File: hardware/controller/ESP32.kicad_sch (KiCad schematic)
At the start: 1 part, among them U1 ESP32-S3

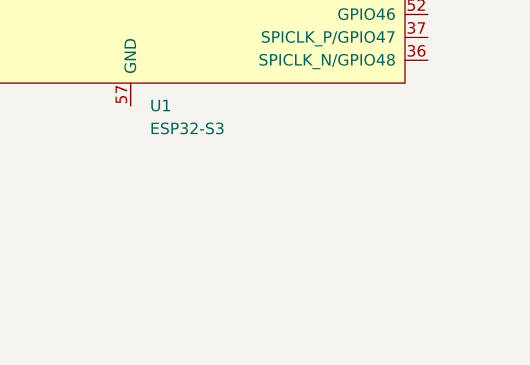
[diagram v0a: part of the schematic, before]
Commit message: added LED IC's and USB UART bridge
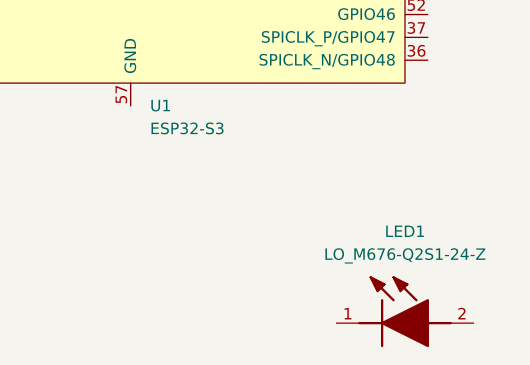
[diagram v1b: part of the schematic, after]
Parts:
- added LED1: LO_M676-Q2S1-24-Z, LEDM2214X140N, symbol SamacSys_Parts:LO_M676-Q2S1-24-Z
- U1: Manufacturer_Part_Number (none) -> ESP32-S3; Mouser Part Number (none) -> 356-ESP32-S3; Mouser Price/Stock (none) -> https://www.mouser.co.uk/ProductDetail/Espressif-Systems/ES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
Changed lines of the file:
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@@
 	(paper "A4")
+	(symbol
+		(lib_id "SamacSys_Parts:LO_M676-Q2S1-24-Z")
+		(at 146.05 153.67 0)
+		(unit 1)
+		(exclude_from_sim no)
+		(in_bom yes)
+		(on_board yes)
+		(dnp no)
+		(fields_autoplaced yes)
+		(property "Reference" "LED1"
+			(at 153.67 143.51 0)
+			(effects
+				(font
+					(size 1.27 1.27)
+				)
+			)
+		)
+		(property "Value" "LO_M676-Q2S1-24-Z"
+			(at 153.67 146.05 0)
+			(effects
+				(font
+					(size 1.27 1.27)
+				)
+			)
+		)
+		(property "Footprint" "LEDM2214X140N"
+			(at 158.75 247.32 0)
+			(effects
+				(font
+					(size 1.27 1.27)
+				)
+				(justify left bottom)
+				(hide yes)
+			)
+		)
+		(property "Datasheet" "https://www.mouser.in/datasheet/2/588/Osram_7222021_LY__M676_EN-2891431.pdf"
+			(at 158.75 347.32 0)
+			(effects
+				(font
+					(size 1.27 1.27)
+				)
+				(justify left bottom)
+				(hide yes)
+			)
+		)
+		(property "Description" "Standard LEDs - SMD Orange, 606nm 224mcd, 20mA"
+			(at 146.05 153.67 0)
+			(effects
+				(font
+					(size 1.27 1.27)
+				)
+				(hide yes)
+			)
+		)
+		(property "Height" "1.4"
+			(at 158.75 547.32 0)
+			(effects
+				(font
+					(size 1.27 1.27)
+				)
+				(justify left bottom)
+				(hide yes)
+			)
+		)
+		(property "Mouser Part Number" "720-LOM676Q2S124Z"
+			(at 158.75 647.32 0)
+			(effects
+				(font
+					(size 1.27 1.27)
+				)
+				(justify left bottom)
+				(hide yes)
+			)
+		)
+		(property "Mouser Price/Stock" "https://www.mouser.co.uk/ProductDetail/OSRAM-Opto-Semiconductors/LO-M676-Q2S1-24-Z?qs=nTDll3UaDK6JlNmxoQCpEQ%3D%3D"
+			(at 158.75 747.32 0)
+			(effects
+				(font
+					(size 1.27 1.27)
+				)
+				(justify left bottom)
+				(hide yes)
+			)
+		)
+		(property "Manufacturer_Name" "ams OSRAM"
+			(at 158.75 847.32 0)
+			(effects
+				(font
+					(size 1.27 1.27)
+				)
+				(justify left bottom)
+				(hide yes)
+			)
+		)
+		(property "Manufacturer_Part_Number" "LO M676-Q2S1-24-Z"
+			(at 158.75 947.32 0)
+			(effects
+				(font
+					(size 1.27 1.27)
+				)
+				(justify left bottom)
+				(hide yes)
+			)
+		)
+		(pin "2"
+		)
+		(pin "1"
+		)
+		(instances
+			(project ""
+				(path "/869bea87-c885-4ead-826b-3f34ceacafad/803675b3-25f7-4b49-b465-4697774a1dce"
+					(reference "LED1")
+					(unit 1)
+				)
+			)
+		)
+	)
 	(symbol
 		(lib_id "Espressif:ESP32-S3")
@@
 			)
 		)
+		(property "Mouser Part Number" "356-ESP32-S3"
+			(at 123.19 88.9 0)
+			(effects
+				(font
+					(size 1.27 1.27)
+				)
+				(hide yes)
+			)
+		)
+		(property "Mouser Price/Stock" "https://www.mouser.co.uk/ProductDetail/Espressif-Systems/ESP32-S3?qs=Rp5uXu7WBW%2FNWuUy%252BBihNw%3D%3D"
+			(at 123.19 88.9 0)
+			(effects
+				(font
+					(size 1.27 1.27)
+				)
+				(hide yes)
+			)
+		)
+		(property "Manufacturer_Part_Number" "ESP32-S3"
+			(at 123.19 88.9 0)
+			(effects
+				(font
+					(size 1.27 1.27)
+				)
+				(hide yes)
+			)
+		)
 		(pin "37"
 		)
@@
 					(unit 1)
 				)
-				(path "/869bea87-c885-4ead-826b-3f34ceacafad/cc3ab021-ec15-450e-9af3-a840a920a1aa"
-					(reference "U4")
-					(unit 1)
-				)

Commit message: asdasd
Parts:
- removed LED1: LO_M676-Q2S1-24-Z, LEDM2214X140N, symbol SamacSys_Parts:LO_M676-Q2S1-24-Z
- renumbered U1 to U2
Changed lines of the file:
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@@
 	(paper "A4")
-	(symbol
-		(lib_id "SamacSys_Parts:LO_M676-Q2S1-24-Z")
-		(at 146.05 153.67 0)
-		(unit 1)
-		(exclude_from_sim no)
-		(in_bom yes)
-		(on_board yes)
-		(dnp no)
-		(fields_autoplaced yes)
-		(property "Reference" "LED1"
-			(at 153.67 143.51 0)
-			(effects
-				(font
-					(size 1.27 1.27)
-				)
-			)
-		)
-		(property "Value" "LO_M676-Q2S1-24-Z"
-			(at 153.67 146.05 0)
-			(effects
-				(font
-					(size 1.27 1.27)
-				)
-			)
-		)
-		(property "Footprint" "LEDM2214X140N"
-			(at 158.75 247.32 0)
-			(effects
-				(font
-					(size 1.27 1.27)
-				)
-				(justify left bottom)
-				(hide yes)
-			)
-		)
-		(property "Datasheet" "https://www.mouser.in/datasheet/2/588/Osram_7222021_LY__M676_EN-2891431.pdf"
-			(at 158.75 347.32 0)
-			(effects
-				(font
-					(size 1.27 1.27)
-				)
-				(justify left bottom)
-				(hide yes)
-			)
-		)
-		(property "Description" "Standard LEDs - SMD Orange, 606nm 224mcd, 20mA"
-			(at 146.05 153.67 0)
-			(effects
-				(font
-					(size 1.27 1.27)
-				)
-				(hide yes)
-			)
-		)
-		(property "Height" "1.4"
-			(at 158.75 547.32 0)
-			(effects
-				(font
-					(size 1.27 1.27)
-				)
-				(justify left bottom)
-				(hide yes)
-			)
-		)
-		(property "Mouser Part Number" "720-LOM676Q2S124Z"
-			(at 158.75 647.32 0)
-			(effects
-				(font
-					(size 1.27 1.27)
-				)
-				(justify left bottom)
-				(hide yes)
-			)
-		)
-		(property "Mouser Price/Stock" "https://www.mouser.co.uk/ProductDetail/OSRAM-Opto-Semiconductors/LO-M676-Q2S1-24-Z?qs=nTDll3UaDK6JlNmxoQCpEQ%3D%3D"
-			(at 158.75 747.32 0)
-			(effects
-				(font
-					(size 1.27 1.27)
-				)
-				(justify left bottom)
-				(hide yes)
-			)
-		)
-		(property "Manufacturer_Name" "ams OSRAM"
-			(at 158.75 847.32 0)
-			(effects
-				(font
-					(size 1.27 1.27)
-				)
-				(justify left bottom)
-				(hide yes)
-			)
-		)
-		(property "Manufacturer_Part_Number" "LO M676-Q2S1-24-Z"
-			(at 158.75 947.32 0)
-			(effects
-				(font
-					(size 1.27 1.27)
-				)
-				(justify left bottom)
-				(hide yes)
-			)
-		)
-		(pin "2"
-		)
-		(pin "1"
-		)
-		(instances
-			(project ""
-				(path "/869bea87-c885-4ead-826b-3f34ceacafad/803675b3-25f7-4b49-b465-4697774a1dce"
-					(reference "LED1")
-					(unit 1)
-				)
-			)
-		)
-	)
 	(symbol
 		(lib_id "Espressif:ESP32-S3")
@@
 		(dnp no)
 		(fields_autoplaced yes)
-		(property "Reference" "U1"
+		(property "Reference" "U2"
 			(at 125.3333 129.54 0)
 			(effects
@@
 			(project "controller"
 				(path "/869bea87-c885-4ead-826b-3f34ceacafad/803675b3-25f7-4b49-b465-4697774a1dce"
-					(reference "U1")
+					(reference "U2")
 					(unit 1)
 				)

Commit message: a
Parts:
- added AE1: Antenna_Chip, symbol Device:Antenna_Chip
- added C1, C4, C5, C6: 0u1, symbol Device:C
- added C11, C12: 1p8, symbol Device:C
- added C2: 10u, symbol Device:C
- added C3, C7: 1u, symbol Device:C
- added C8, C9: 10p, symbol Device:C
- added J5: Conn_01x04_Pin, symbol Connector:Conn_01x04_Pin
- added L1: 2nH, symbol Device:L
- added L2: 24n, symbol Device:L
- added L4: 3nH, symbol Device:L
- added Q1, Q2: SS8050-G, SOT95P240X115-3N, symbol SamacSys_Parts:SS8050-G
- added R23, R24: 10k, symbol Device:R
- added Y2: FH4000074Z, FH4000074Z, symbol SamacSys_Parts:FH4000074Z
- U2: symbol Espressif:ESP32-S3 -> SamacSys_Parts:ESP32-S3
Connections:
- net VDD3P3: now also C5.1, L1.2
- net at U2.1 (LNA_IN/RF): now also C12.1, L4.2
- net +3V3: now reaches U2.20 (VDD3P3_RTC)
- net +3V3: now also U2.55 (VDDA), U2.56 (VDDA), C1.1, C2.1, C3.1, C4.1, L1.1
- net VDD_SPI: now reaches U2.29 (VDD_SPI)
- net VDD_SPI: now also C6.1, C7.1
- net CHIP_PU: now reaches U2.4 (CHIP_PU/RESET)
- net MTCK: now reaches U2.44 (MTCK/JTAG/GPIO39)
- net MTCK: now also J5.4 (Pin_4)
- net MTDO: now reaches U2.45 (MTDO/JTAG/GPIO40)
- net MTDO: now also J5.3 (Pin_3)
- net at U2.46 (VDD3P3_CPU): now also C1.2
- net MTDI: now reaches U2.47 (MTDI/JTAG/GPIO41)
- net MTDI: now also J5.2 (Pin_2)
- net MTMS: now reaches U2.48 (MTMS/JTAG/GPIO42)
- net MTMS: now also J5.1 (Pin_1)
- net at U2.53 (XTAL_N): now also C8.1, Y2.3 (XOUT)
- net at U2.54 (XTAL_P): now also L2.2
- net GND: now reaches U2.57 (GND)
- net GND: now also AE1.1 (FEED), C11.2, C12.2, C2.2, C3.2, C4.2, C5.2, C6.2, C7.2, C8.2, C9.2, Y2.2 (GND), Y2.4 (GND)
- new net: Q2.1 (B), R24.2
- new net: AE1.2 (PCB_Trace), C11.1, L4.1
- new net: C9.1, L2.1, Y2.1 (XIN)
- new net: Q1.1 (B), R23.2
- new net DTR: Q1.3 (C), R24.1
- new net EN: Q2.3 (C)
- new net IO0: Q1.2 (E)
- new net RTS: Q2.2 (E), R23.1
- no-connect marks 0 -> 2
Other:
- note added: "Auto-flash"
- note added: "JTAG Interface"
- note added: "todo: expose jtag port"
- note added: "todo: look into why some of these power pins do not hvae any decouplihg caps"
- moved on the sheet: U2

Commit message: fixed bus stuff
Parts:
- renumbered C8 to C1, C5 to C10, C1 to C11, C9 to C2, C2 to C3, C11 to C4, C12 to C5, C3 to C6, C6 to C7, C4 to C8, C7 to C9, J5 to J4, L4 to L1, L1 to L3, Q2 to Q1, Q1 to Q2, R23 to R10, R24 to R9, Y2 to Y1
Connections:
- net BUT_JOY.BUT_DOWN: now also U2.15 (GPIO10/ADC1_CH9)
- net BUT_JOY.BUT_LEFT: now also U2.12 (GPIO7/ADC1_CH6)
- net BUT_JOY.BUT_RIGHT: now also U2.13 (GPIO8/ADC1_CH7)
- net BUT_JOY.BUT_UP: now also U2.14 (GPIO9/ADC1_CH8)
- net BUT_JOY.JOY1_H: now also U2.11 (GPIO6/ADC1_CH5)
- net BUT_JOY.JOY1_V: now also U2.10 (GPIO5/ADC1_CH4)
- net BUT_JOY.JOY2_H: now also U2.9 (GPIO4/ADC1_CH3)
- net BUT_JOY.JOY2_V: now also U2.8 (GPIO3/ADC1_CH2)
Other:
- note added: "JTAG Interface Male Headers"
- note removed: "JTAG Interface"
- moved on the sheet: J4

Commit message: bussin
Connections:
- net RXD: now also U2.50 (U0RXD/PROG/GPIO44)
- net TXD: now also U2.49 (U0TXD/PROG/GPIO43)
- net ~{CE}: now reaches U2.28 (SPI_CS1/GPIO26)
- net DQ3: now reaches U2.30 (SPIHD/GPIO27)
- net DQ2: now reaches U2.31 (SPIWP/GPIO28)
- net ~{CS}: now reaches U2.32 (SPICS0/GPIO29)
- net OPI_CLK: now reaches U2.33 (SPICLK/GPIO30)
- net DQ1: now reaches U2.34 (SPIQ/GPIO31)
- net DQ0: now reaches U2.35 (SPID/GPIO32)
- net DQ4: now reaches U2.38 (GPIO33)
- net DQ5: now reaches U2.39 (GPIO34)
- net DQ6: now reaches U2.40 (GPIO35)
- net DQ7: now reaches U2.41 (GPIO36)
- net DQS/DM: now reaches U2.42 (GPIO37)

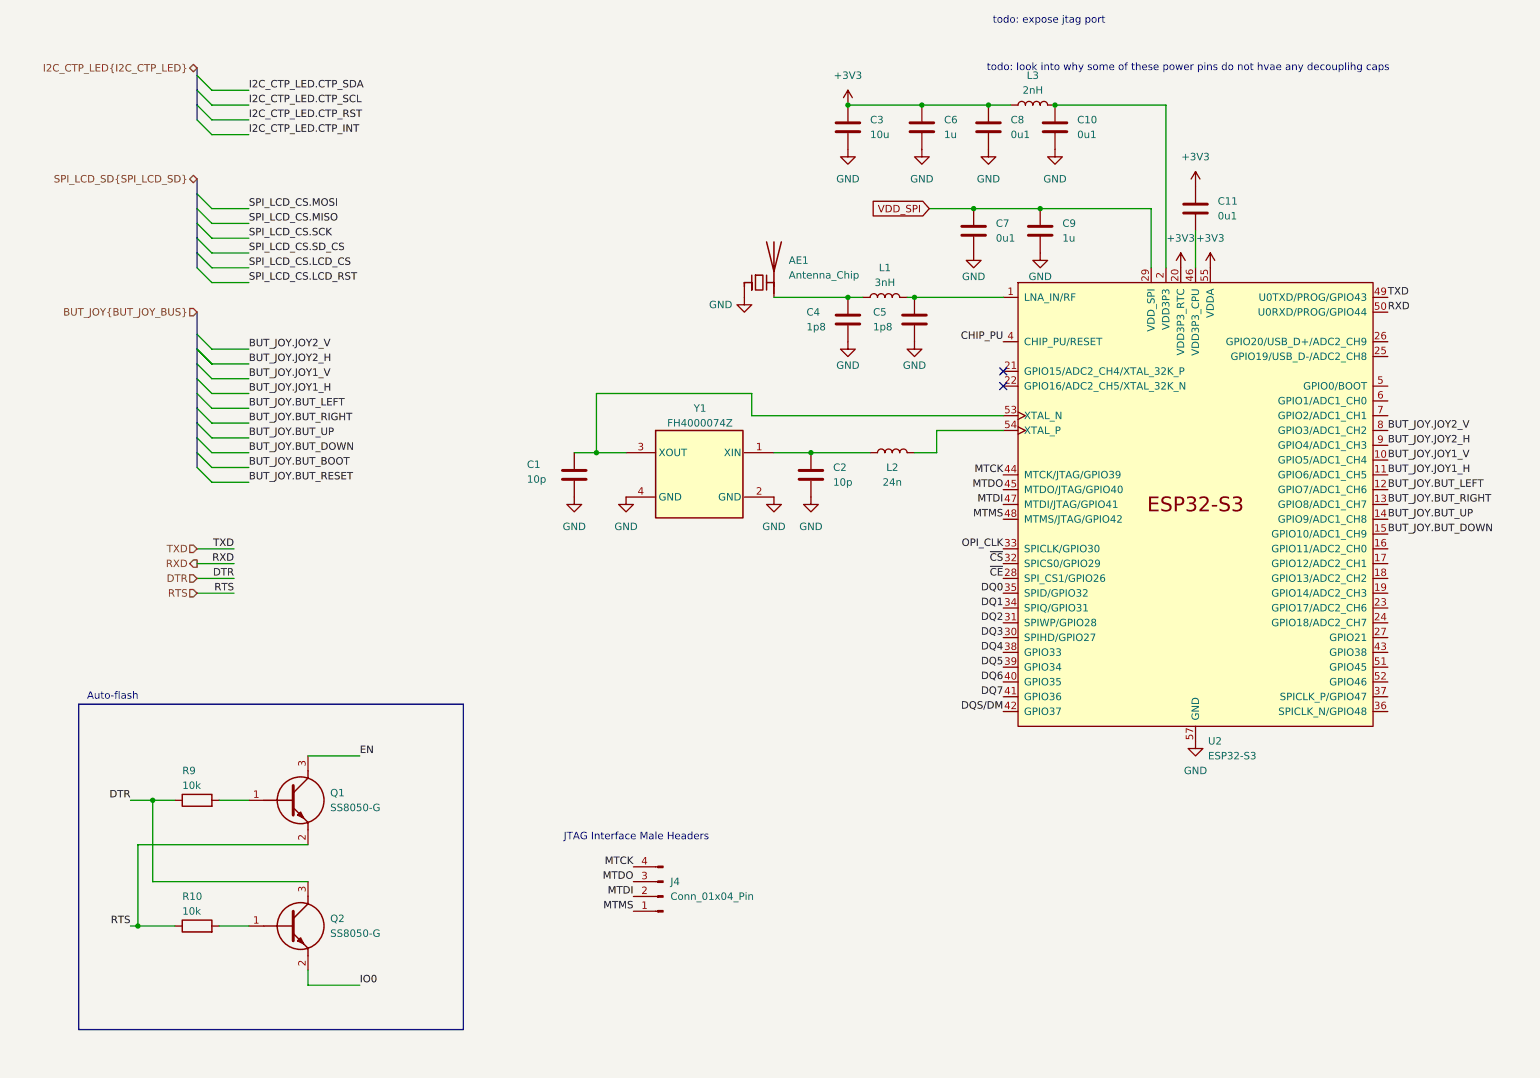
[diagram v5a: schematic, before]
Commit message: added memory and fixed gpio pins
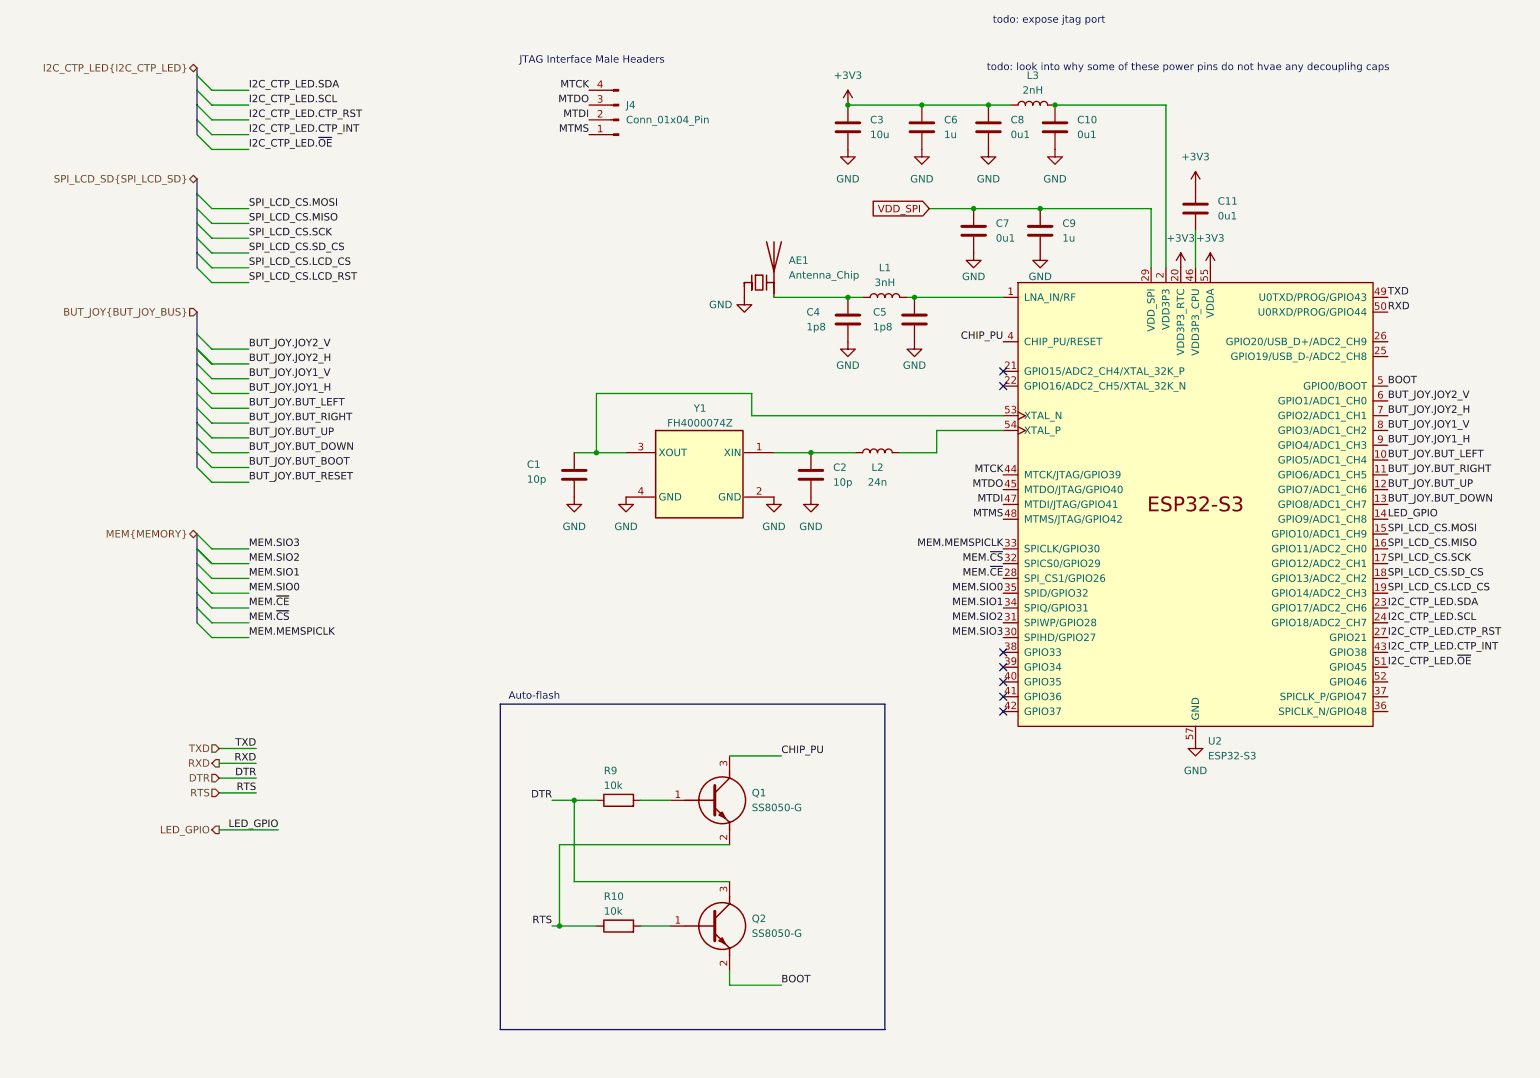
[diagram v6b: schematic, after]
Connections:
- net EN is gone; now on net CHIP_PU: Q1.3 (C)
- net IO0 is gone; now on net BOOT: Q2.2 (E)
- net BUT_JOY.BUT_DOWN: now also U2.13 (GPIO8/ADC1_CH7); no longer U2.15 (GPIO10/ADC1_CH9)
- net BUT_JOY.BUT_LEFT: now also U2.10 (GPIO5/ADC1_CH4); no longer U2.12 (GPIO7/ADC1_CH6)
- net BUT_JOY.BUT_RIGHT: now also U2.11 (GPIO6/ADC1_CH5); no longer U2.13 (GPIO8/ADC1_CH7)
- net BUT_JOY.BUT_UP: now also U2.12 (GPIO7/ADC1_CH6); no longer U2.14 (GPIO9/ADC1_CH8)
- net BUT_JOY.JOY1_H: now also U2.9 (GPIO4/ADC1_CH3); no longer U2.11 (GPIO6/ADC1_CH5)
- net BUT_JOY.JOY1_V: now also U2.8 (GPIO3/ADC1_CH2); no longer U2.10 (GPIO5/ADC1_CH4)
- net BUT_JOY.JOY2_H: now also U2.7 (GPIO2/ADC1_CH1); no longer U2.9 (GPIO4/ADC1_CH3)
- net BUT_JOY.JOY2_V: now also U2.6 (GPIO1/ADC1_CH0); no longer U2.8 (GPIO3/ADC1_CH2)
- net I2C_CTP_LED.CTP_INT: now also U2.43 (GPIO38)
- net I2C_CTP_LED.CTP_RST: now also U2.27 (GPIO21)
- net SPI_LCD_CS.LCD_CS: now also U2.19 (GPIO14/ADC2_CH3)
- net SPI_LCD_CS.MISO: now also U2.16 (GPIO11/ADC2_CH0)
- net SPI_LCD_CS.MOSI: now also U2.15 (GPIO10/ADC1_CH9)
- net SPI_LCD_CS.SCK: now also U2.17 (GPIO12/ADC2_CH1)
- net SPI_LCD_CS.SD_CS: now also U2.18 (GPIO13/ADC2_CH2)
- net I2C_CTP_LED.SDA: now reaches U2.23 (GPIO17/ADC2_CH6)
- net I2C_CTP_LED.SCL: now reaches U2.24 (GPIO18/ADC2_CH7)
- net BOOT: now reaches U2.5 (GPIO0/BOOT)
- net I2C_CTP_LED.~{OE}: now reaches U2.51 (GPIO45)
- net DQ0 renamed MEM.SIO0
- net DQ1 renamed MEM.SIO1
- net DQ2 renamed MEM.SIO2
- net DQ3 renamed MEM.SIO3
- net DQ4: no longer names the net of U2.38 (GPIO33)
- net DQ5: no longer names the net of U2.39 (GPIO34)
- net DQ6: no longer names the net of U2.40 (GPIO35)
- net DQ7: no longer names the net of U2.41 (GPIO36)
- net DQS/DM: no longer names the net of U2.42 (GPIO37)
- net OPI_CLK renamed MEM.MEMSPICLK
- net ~{CE} renamed MEM.~{CE}
- net ~{CS} renamed MEM.~{CS}
- new net LED_GPIO: U2.14 (GPIO9/ADC1_CH8)
- no-connect marks 2 -> 7
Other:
- moved on the sheet: J4, L2, Q1, Q2, R10, R9

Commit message: lol
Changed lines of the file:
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@@
 	(wire
 		(pts
-			(xy 57.15 153.67) (xy 46.99 153.67)
+			(xy 55.88 143.51) (xy 45.72 143.51)
 		)
 		(stroke
@@
 	(wire
 		(pts
-			(xy 46.99 147.32) (xy 53.34 147.32)
+			(xy 45.72 137.16) (xy 52.07 137.16)
 		)
 		(stroke
@@
 	(wire
 		(pts
-			(xy 46.99 144.78) (xy 53.34 144.78)
+			(xy 45.72 134.62) (xy 52.07 134.62)
 		)
 		(stroke
@@
 	(wire
 		(pts
-			(xy 46.99 139.7) (xy 53.34 139.7)
+			(xy 45.72 129.54) (xy 52.07 129.54)
 		)
 		(stroke
@@
 	(wire
 		(pts
-			(xy 46.99 142.24) (xy 53.34 142.24)
+			(xy 45.72 132.08) (xy 52.07 132.08)
 		)
 		(stroke
@@
 	)
 	(label "RTS"
-		(at 53.34 147.32 180)
+		(at 52.07 137.16 180)
 		(effects
 			(font
@@
 	)
 	(label "DTR"
-		(at 53.34 144.78 180)
+		(at 52.07 134.62 180)
 		(effects
 			(font
@@
 	)
 	(label "TXD"
-		(at 53.34 139.7 180)
+		(at 52.07 129.54 180)
 		(effects
 			(font
@@
 	)
 	(label "RXD"
-		(at 53.34 142.24 180)
+		(at 52.07 132.08 180)
 		(effects
 			(font
@@
 	)
 	(label "LED_GPIO"
-		(at 57.15 153.67 180)
+		(at 55.88 143.51 180)
 		(effects
 			(font
@@
 	(hierarchical_label "LED_GPIO"
 		(shape output)
-		(at 46.99 153.67 180)
+		(at 45.72 143.51 180)
 		(effects
 			(font
@@
 	(hierarchical_label "RTS"
 		(shape input)
-		(at 46.99 147.32 180)
+		(at 45.72 137.16 180)
 		(effects
 			(font
@@
 	(hierarchical_label "RXD"
 		(shape output)
-		(at 46.99 142.24 180)
+		(at 45.72 132.08 180)
 		(effects
 			(font
@@
 	(hierarchical_label "DTR"
 		(shape input)
-		(at 46.99 144.78 180)
+		(at 45.72 134.62 180)
 		(effects
 			(font
@@
 	(hierarchical_label "TXD"
 		(shape input)
-		(at 46.99 139.7 180)
-		(effects
-			(font
+		(at 45.72 129.54 180)
+		(effects
+			(font
